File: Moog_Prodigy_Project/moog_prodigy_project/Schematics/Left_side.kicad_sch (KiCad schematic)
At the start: 85 parts, among them Q1 CA3046, Q15 BC549, Q2 CA3046, Q4 CA3046, Q6 BC549, U11 +12V, U12 +12V, U15 +12V, U16 +12V, U17 +12V, U18 +12V, U19 +12V, U20 +12V, U21 +12V, U2A1 OPA134, U2B3 OPA134, U3 +12V, U4 +12V, U41 +12V, U5 NE5532, U55 -12V, U56 -12V, U57 -12V, U58 -12V, U59 -12V, U6 LT1011CN8, U60 -12V, U61 -12V, U62 -12V, U63 -12V, U64 +12V, U65 +12V, U66 -12V, U7 AD8066ARM, U8 NE5532

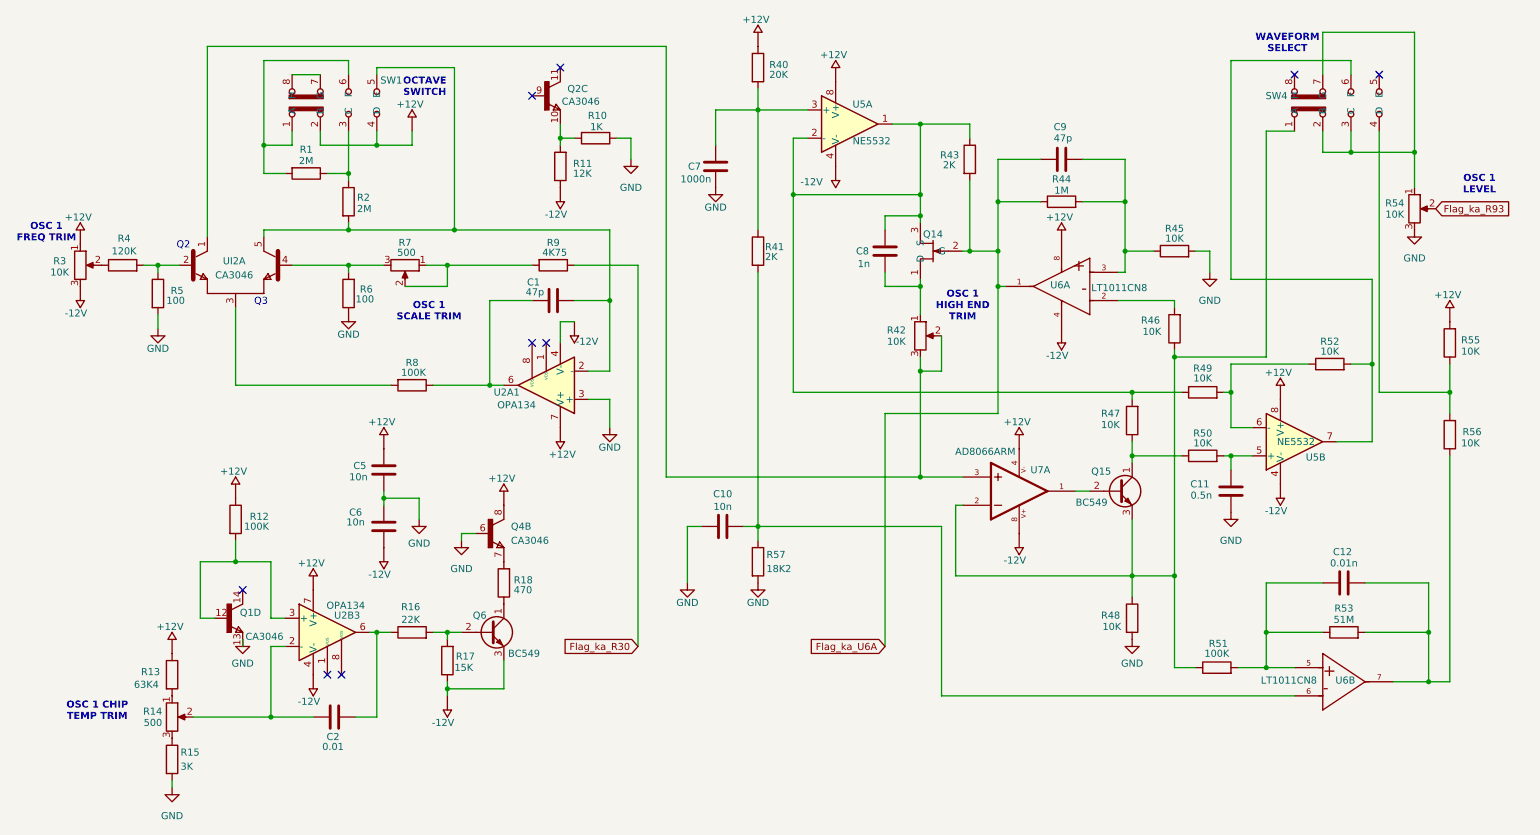
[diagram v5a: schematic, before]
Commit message: Footprint update new 28.04.2026
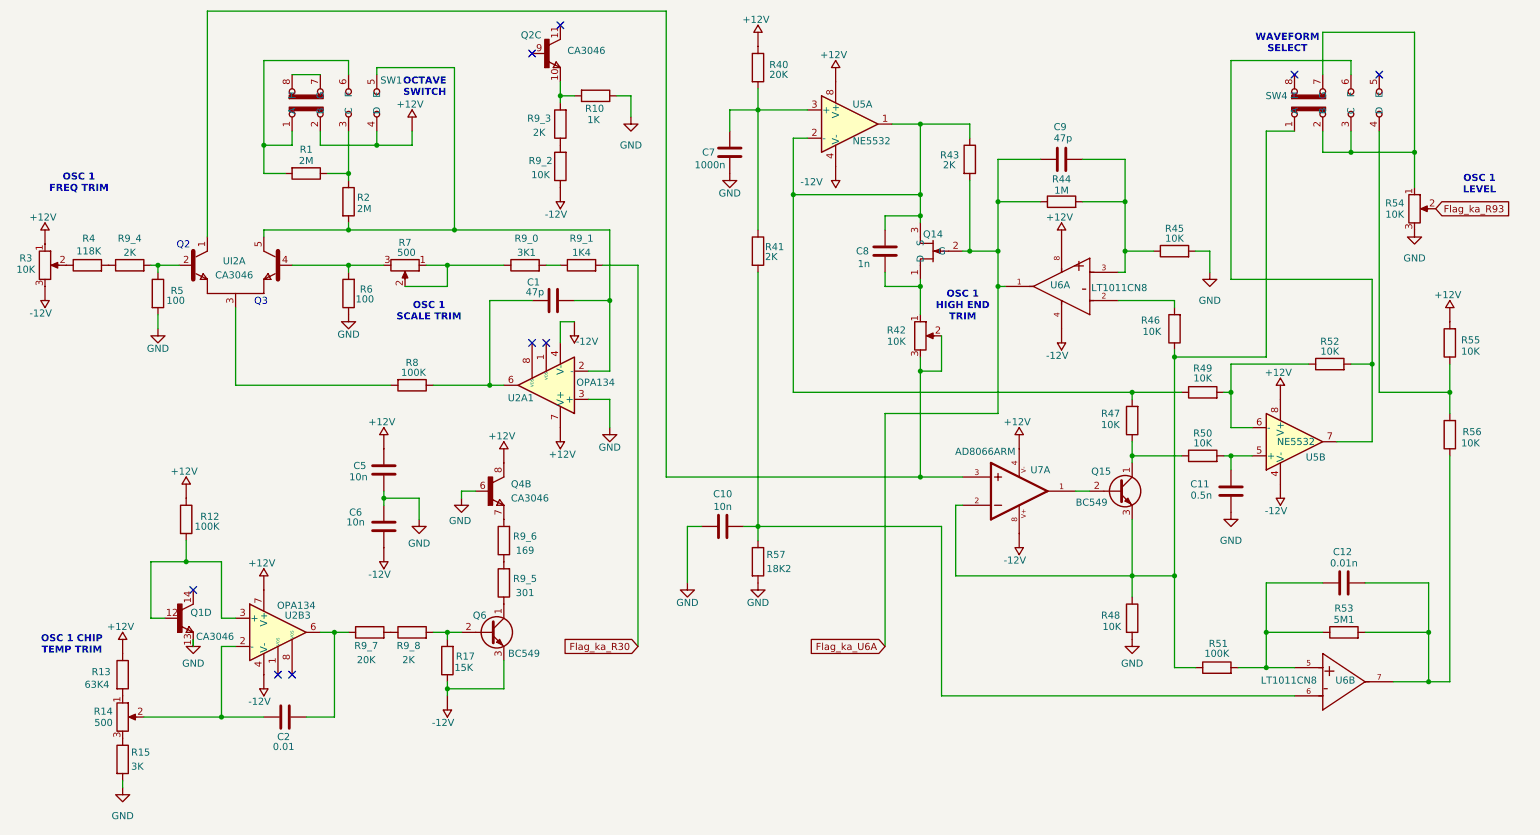
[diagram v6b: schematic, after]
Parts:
- removed R11: 12K, symbol Device:R
- removed R16: 22K, symbol Device:R
- removed R18: 470, symbol Device:R
- removed R9: 4K75, symbol Device:R
- added R9_0: 3K1, Resistor_THT:R_Axial_DIN0207_L6.3mm_D2.5mm_P10.16mm_Horizontal, symbol Device:R
- added R9_1: 1K4, Resistor_THT:R_Axial_DIN0207_L6.3mm_D2.5mm_P10.16mm_Horizontal, symbol Device:R
- added R9_2: 10K, Resistor_THT:R_Axial_DIN0207_L6.3mm_D2.5mm_P10.16mm_Horizontal, symbol Device:R
- added R9_3, R9_4, R9_8: 2K, Resistor_THT:R_Axial_DIN0207_L6.3mm_D2.5mm_P10.16mm_Horizontal, symbol Device:R
- added R9_5: 301, Resistor_THT:R_Axial_DIN0207_L6.3mm_D2.5mm_P10.16mm_Horizontal, symbol Device:R
- added R9_6: 169, Resistor_THT:R_Axial_DIN0207_L6.3mm_D2.5mm_P10.16mm_Horizontal, symbol Device:R
- added R9_7: 20K, Resistor_THT:R_Axial_DIN0207_L6.3mm_D2.5mm_P10.16mm_Horizontal, symbol Device:R
- C1, C10, C11, C12, C2, C5, C6, C8, C9: footprint (none) -> Capacitor_THT:C_Disc_D5.0mm_W2.5mm_P2.50mm
- C7: footprint (none) -> Capacitor_THT:CP_Radial_D5.0mm_P2.00mm
- Q1, Q2, Q4: footprint (none) -> CA3046:DIL14
- Q14: value ~ -> BF256C
- R1, R10, R12, R13, R14, R15, R17, R2, R3, R40, R41, R42, R43, R44, R45, R46, R47, R48, R49, R5, R50, R51, R52, R54, R55, R56, R57, R6, R7, R8: footprint (none) -> Resistor_THT:R_Axial_DIN0207_L6.3mm_D2.5mm_P10.16mm_Horizontal
- R4: value 120K -> 118K; footprint (none) -> Resistor_THT:R_Axial_DIN0207_L6.3mm_D2.5mm_P10.16mm_Horizontal
- R53: value 51M -> 5M1; footprint (none) -> Resistor_THT:R_Axial_DIN0207_L6.3mm_D2.5mm_P10.16mm_Horizontal
- SW1, SW4: value ~ -> 4x4; footprint (none) -> SLW-1575662-5A-S-D_Switch_4x4:SW_SLW-1575662-5A-S-D
- U5, U8: footprint (none) -> NE5532AP:DIP794W45P254L1016H508Q8
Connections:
- net Flag_ka_R30: now also R9_1.2
- net at U61.: now also R9_2.1
- net at R7.1, R7.2: now also R9_0.1
- net at R5.1, UI2.2: now also R9_4.2; no longer R4.2
- net at Q6.1 (C): now also R9_5.1
- net at Q6.2 (B), R17.2: now also R9_8.2
- net at Q4.7: now also R9_6.2
- net at Q2.10, R10.2: now also R9_3.2
- net at C2.2, U2B3.6: now also R9_7.1
- new net: R9_5.2, R9_6.1
- new net: R9_0.2, R9_1.1
- new net: R9_2.2, R9_3.1
- new net: R9_7.2, R9_8.1
- new net: R4.2, R9_4.1
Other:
- moved on the sheet: C2, C7, Q1D, Q4B, R10, R12, R13, R14, R15, R3, R4, U2B3

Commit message: Footprints import new 29.04.2026
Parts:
- U2A1, U2B3: footprint (none) -> OPA134PA:DIP794W45P254L959H508Q8
- U6: footprint Package_DIP:DIP-8_W7.62mm_Socket -> L101011ML04Q_1x1:SW_L101011ML04Q
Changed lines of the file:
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@@
 			)
 		)
-		(property "Footprint" ""
+		(property "Footprint" "OPA134PA:DIP794W45P254L959H508Q8"
 			(at 106.68 83.82 0)
 			(effects
@@
 			)
 		)
-		(property "Footprint" "Package_DIP:DIP-8_W7.62mm_Socket"
+		(property "Footprint" "L101011ML04Q_1x1:SW_L101011ML04Q"
 			(at 210.82 62.23 0)
 			(effects
@@
 			)
 		)
-		(property "Footprint" ""
+		(property "Footprint" "OPA134PA:DIP794W45P254L959H508Q8"
 			(at 60.96 125.73 0)
 			(effects
@@
 			)
 		)
-		(property "Footprint" "Package_DIP:DIP-8_W7.62mm_Socket"
+		(property "Footprint" "L101011ML04Q_1x1:SW_L101011ML04Q"
 			(at 242.57 133.35 0)
 			(effects
